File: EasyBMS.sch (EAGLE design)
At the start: 147 parts, among them Q1 BSS84LT1G, Q10 BSS84LT1G, Q11 BSS84LT1G, Q12 BSS84LT1G, Q14 BSS84LT1G, Q3 BSS84LT1G, Q4 BSS84LT1G, Q5 BSS84LT1G, Q6 BSS84LT1G, Q7 BSS84LT1G, Q8 BSS84LT1G, Q9 BSS84LT1G

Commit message: minimize board size to 100x32
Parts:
- removed JP10: (no value), pinhead:PINHD-1X10
- removed JP5, JP6: (no value), pinhead:PINHD-2X24
- removed JP7, JP8: (no value), pinhead:PINHD-1X24
- added JP11: (no value), pinhead_own:PINHD-2X24
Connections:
- removed net N$10: JP5.42, JP7.21
- removed net N$100: JP6.31, JP8.16
- removed net N$101: JP6.29, JP8.15
- removed net N$102: JP6.27, JP8.14
- removed net N$103: JP6.25, JP8.13
- removed net N$104: JP6.23, JP8.12
- removed net N$105: JP6.21, JP8.11
- removed net N$107: JP6.19, JP8.10
- removed net N$108: JP6.17, JP8.9
- removed net N$109: JP6.15, JP8.8
- removed net N$11: JP5.40, JP7.20
- removed net N$110: JP6.13, JP8.7
- removed net N$111: JP6.11, JP8.6
- removed net N$112: JP6.9, JP8.5
- removed net N$113: JP6.7, JP8.4
- removed net N$114: JP6.5, JP8.3
- removed net N$115: JP6.3, JP8.2
- removed net N$116: JP6.1, JP8.1
- removed net N$118: JP5.2, JP7.1
- removed net N$12: JP5.38, JP7.19
- removed net N$13: JP5.36, JP7.18
- removed net N$21: JP5.34, JP7.17
- removed net N$24: JP5.32, JP7.16
- removed net N$61: JP5.30, JP7.15
- removed net N$74: JP5.28, JP7.14
- removed net N$75: JP5.26, JP7.13
- removed net N$76: JP5.24, JP7.12
- removed net N$77: JP5.22, JP7.11
- removed net N$78: JP5.20, JP7.10
- removed net N$8: JP5.46, JP7.23
- removed net N$84: JP5.18, JP7.9
- removed net N$85: JP5.16, JP7.8
- removed net N$86: JP5.14, JP7.7
- removed net N$87: JP5.12, JP7.6
- removed net N$88: JP5.10, JP7.5
- removed net N$89: JP5.8, JP7.4
- removed net N$9: JP5.44, JP7.22
- removed net N$90: JP5.6, JP7.3
- removed net N$91: JP5.4, JP7.2
- removed net N$92: JP6.47, JP8.24
- removed net N$93: JP6.45, JP8.23
- removed net N$94: JP6.43, JP8.22
- removed net N$95: JP6.41, JP8.21
- removed net N$96: JP6.39, JP8.20
- removed net N$97: JP6.37, JP8.19
- removed net N$98: JP6.35, JP8.18
- removed net N$99: JP6.33, JP8.17
- new net C: C4.1, R19.1
- new net LOWER: C4.2, R17.1, R82.2
- new net S: R13.1
- new net UPPERCELL: Q1.S, R19.2
- net C0: now also JP11.46; no longer JP6.46
- net C1: now also JP11.47; no longer C4.1, JP5.47, R19.1
- net C10: now also JP11.11; no longer JP5.11
- net C11: now also JP11.7; no longer JP5.7
- net C12: now also JP11.3; no longer JP5.3
- net C2: now also JP11.43; no longer JP5.43
- net C3: now also JP11.39; no longer JP5.39
- net C4: now also JP11.35; no longer JP5.35
- net C5: now also JP11.31; no longer JP5.31
- net C6: now also JP11.27; no longer JP5.27
- net C7: now also JP11.23; no longer JP5.23
- net C8: now also JP11.19; no longer JP5.19
- net C9: now also JP11.15; no longer JP5.15
- net CSB: now also JP11.16; no longer JP6.16
- net DRIVE: now also JP11.22; no longer JP6.22
- net GND: now also JP11.18, JP11.36, JP11.38; no longer C4.2, C5.2, D3.A, JP10.1, JP10.10, JP10.2, JP10.3, JP10.4, JP10.5, JP10.6, JP10.7, JP10.8, JP10.9, JP6.18, JP6.36, JP6.38, R17.1, R3.2, R82.2
- net GPIO1: now also JP11.44; no longer JP6.44
- net GPIO2: now also JP11.42; no longer JP6.42
- net GPIO3: now also JP11.40; no longer JP6.40
- net GPIO4: now also JP11.34; no longer JP6.34
- net GPIO5: now also JP11.32; no longer JP6.32
- net ICMP: now also JP11.6, JP11.8; no longer JP6.6, JP6.8
- net IMB: now also JP11.4; no longer JP6.4
- net IPB: now also JP11.2; no longer JP6.2
- net MISO: now also JP11.10; no longer JP6.10
- net MOSI: now also JP11.12; no longer JP6.12
- net N$7: now also R3.2; no longer JP5.48, JP7.24
- net P13: now also JP11.1; no longer JP5.1
- net P2: no longer D3.K, Q1.S, R19.2
- net S1: now also JP11.48; no longer JP6.48, R13.1
- net S10: now also JP11.13; no longer JP5.13
- net S11: now also JP11.9; no longer JP5.9
- net S12: now also JP11.5; no longer JP5.5
- net S2: now also JP11.45; no longer JP5.45
- net S3: now also JP11.41; no longer JP5.41
- net S4: now also JP11.37; no longer JP5.37
- net S5: now also JP11.33; no longer JP5.33
- net S6: now also JP11.29; no longer JP5.29
- net S7: now also JP11.25; no longer JP5.25
- net S8: now also JP11.21; no longer JP5.21
- net S9: now also JP11.17; no longer JP5.17
- net SCK: now also JP11.14; no longer JP6.14
- net SWTEN: now also JP11.26; no longer JP6.26
- net VREF1: now also JP11.28; no longer JP6.28
- net VREF2: now also JP11.30; no longer JP6.30
- net VREG: now also JP11.24; no longer JP6.24
- net WDT: now also JP11.20; no longer JP6.20
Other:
- moved on the sheet: C5, R3

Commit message: size changed to 100x49
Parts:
- removed C4: (no value), rcl:C-EUC0402
- removed LED10, LED18: KT-0603R, led:LEDCHIPLED_0603
- removed Q1, Q14: BSS84LT1G, SamacSys_Parts:BSS84LT1G
- removed R100, R19: 100R, rcl:R-EU_R0402
- removed R13, R98: 3.3k, rcl:R-EU_R0402
- removed R17, R18, R9, R96, R97: 10R0, rcl:R-EU_R1206
- removed R82, R99: 470R, rcl:R-EU_R0402
- added C16: (no value), rcl:C-EUC0402
- added LED17, LED5: KT-0603R, led:LEDCHIPLED_0603
- added Q13, Q2: BSS84LT1G, SamacSys_Parts:BSS84LT1G
- added R10, R93: 3.3k, rcl:R-EU_R0402
- added R11, R94: 470R, rcl:R-EU_R0402
- added R4, R7, R8, R90, R91, R92: 10R0, rcl:R-EU_R1206
- added R89: 100R, rcl:R-EU_R0402
- R12, R24, R30, R36, R42, R48, R64, R70, R76, R83, R95: value 10R0 -> 100R; device rcl:R-EU_R1206 -> rcl:R-EU_R0402
- R21, R27, R33, R39, R45, R51, R67, R73, R79, R86: value 3.3k -> 10R0; device rcl:R-EU_R0402 -> rcl:R-EU_R1206
- R22, R28, R34, R40, R46, R52, R68, R74, R80, R87: value 470R -> 3.3k
- R23, R29, R35, R41, R47, R63, R69, R75, R81, R88: value 100R -> 470R
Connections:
- removed net C: C4.1, R19.1
- removed net LOWER: C4.2, R17.1, R82.2
- removed net N$15: R18.2, R9.1
- removed net N$157: LED10.C, R82.1
- removed net N$17: R17.2, R18.1
- removed net N$18: LED10.A, Q1.D, R9.2
- removed net N$25: Q1.G, R13.2
- removed net N$27 (its old number): LED7.A, Q4.D, R26.2
- removed net N$33 (its old number): LED8.A, Q5.D, R32.2
- removed net N$38 (its old number): LED9.A, Q6.D, R38.2
- removed net N$43 (its old number): LED11.A, Q7.D, R44.2
- removed net N$48 (its old number): LED12.A, Q8.D, R50.2
- removed net N$53 (its old number): LED13.A, Q9.D, R66.2
- removed net N$58 (its old number): LED14.A, Q10.D, R72.2
- removed net N$7: R3.2
- removed net N$79: R95.2, R96.1
- removed net N$80: R96.2, R97.1
- removed net N$81: LED18.A, Q14.D, R97.2
- removed net N$82: Q14.G, R98.2
- removed net N$83: LED18.C, R99.1
- removed net S: R13.1
- removed net UPPERCELL: Q1.S, R19.2
- new net N$10: LED5.A, Q2.D, R8.2
- new net N$11: Q2.G, R10.2
- new net N$12: LED5.C, R11.1
- new net N$16: LED6.A, Q3.D, R21.2
- new net N$24: Q4.G, R28.2
- new net N$26: LED7.C, R29.1
- new net N$32: LED8.C, R35.1
- new net N$37: LED9.C, R41.1
- new net N$42: LED11.C, R47.1
- new net N$47: LED12.C, R63.1
- new net N$52: LED13.C, R69.1
- new net N$57: LED14.C, R75.1
- new net N$61: Q11.G, R80.2
- new net N$68: R90.2, R91.1
- new net N$74: LED17.C, R94.1
- new net N$8: R4.2, R7.1
- new net N$9: R7.2, R8.1
- net C1: now also C6.1, R12.1
- net C10: now also C15.1, R83.1; no longer C17.1, R100.1
- net C11: now also C16.1, R89.1; no longer C12.1, R69.1
- net C12: now also C17.1, R95.1; no longer C14.1, R81.1
- net C2: now also C7.1, R24.1; no longer C6.1, R23.1
- net C3: now also C9.1, R36.1; no longer C7.1, R29.1
- net C4: now also R30.1; no longer R35.1
- net C5: now also C10.1, R42.1; no longer C9.1, R41.1
- net C6: now also C11.1, R48.1; no longer C10.1, R47.1
- net C7: now also C12.1, R64.1; no longer C11.1, R63.1
- net C8: now also R70.1; no longer R75.1
- net C9: now also C14.1, R76.1; no longer C15.1, R88.1
- net GND: now also C5.2, C6.2, D3.A, R11.2, R3.2, R4.1
- net N$14: now also R20.2, R21.1; no longer R12.2, R14.1
- net N$19: now also Q3.G, R22.2; no longer LED6.A, Q3.D, R20.2
- net N$20: now also LED6.C, R23.1; no longer Q3.G, R21.2
- net N$22: now also R26.2, R27.1; no longer LED6.C, R22.1
- net N$23: now also LED7.A, Q4.D, R27.2; no longer R24.2, R25.1
- net N$28: now also R32.2, R33.1; no longer Q4.G, R27.2
- net N$29: now also LED8.A, Q5.D, R33.2; no longer LED7.C, R28.1
- net N$31: now also Q5.G, R34.2; no longer R30.2, R31.1
- net N$34: now also R38.2, R39.1; no longer Q5.G, R33.2
- net N$35: now also LED9.A, Q6.D, R39.2; no longer LED8.C, R34.1
- net N$36: now also Q6.G, R40.2; no longer R36.2, R37.1
- net N$39: now also R44.2, R45.1; no longer Q6.G, R39.2
- net N$40: now also LED11.A, Q7.D, R45.2; no longer LED9.C, R40.1
- net N$41: now also Q7.G, R46.2; no longer R42.2, R43.1
- net N$44: now also R50.2, R51.1; no longer Q7.G, R45.2
- net N$45: now also LED12.A, Q8.D, R51.2; no longer LED11.C, R46.1
- net N$46: now also Q8.G, R52.2; no longer R48.2, R49.1
- net N$49: now also R66.2, R67.1; no longer Q8.G, R51.2
- net N$50: now also LED13.A, Q9.D, R67.2; no longer LED12.C, R52.1
- net N$51: now also Q9.G, R68.2; no longer R64.2, R65.1
- net N$54: now also R72.2, R73.1; no longer Q9.G, R67.2
- net N$55: now also LED14.A, Q10.D, R73.2; no longer LED13.C, R68.1
- net N$56: now also Q10.G, R74.2; no longer R70.2, R71.1
- net N$59: now also R78.2, R79.1; no longer Q10.G, R73.2
- net N$60: now also LED15.A, Q11.D, R79.2; no longer LED14.C, R74.1
- net N$62: now also LED15.C, R81.1; no longer R76.2, R77.1
- net N$64: now also R85.2, R86.1; no longer LED15.A, Q11.D, R78.2
- net N$65: now also LED16.A, Q12.D, R86.2; no longer Q11.G, R79.2
- net N$66: now also Q12.G, R87.2; no longer LED15.C, R80.1
- net N$67: now also LED16.C, R88.1; no longer R83.2, R84.1
- net N$69: now also R91.2, R92.1; no longer LED16.A, Q12.D, R85.2
- net N$71: now also LED17.A, Q13.D, R92.2; no longer Q12.G, R86.2
- net N$72: now also Q13.G, R93.2; no longer LED16.C, R87.1
- net P10: now also C15.2, Q10.S, R76.2, R77.1, R81.2; no longer C17.2, Q12.S, R88.2, R95.1, R99.2
- net P11: now also C16.2, Q11.S, R83.2, R84.1, R88.2; no longer C12.2, Q14.S, R100.2, R64.1, R68.2
- net P12: now also C17.2, Q12.S, R89.2, R90.1, R94.2; no longer C14.2, Q9.S, R69.2, R76.1, R80.2
- net P13: now also Q13.S, R95.2; no longer Q11.S, R81.2
- net P2: now also C7.2, D3.K, Q2.S, R12.2, R14.1, R23.2; no longer C6.2, R12.1, R22.2
- net P3: now also C9.2, R24.2, R31.1, R35.2; no longer C7.2, R23.2, R24.1, R28.2
- net P4: now also Q5.S, R25.1, R36.2; no longer Q4.S, R30.1, R34.2
- net P5: now also C10.2, Q4.S, R30.2, R37.1, R41.2; no longer C9.2, Q5.S, R35.2, R36.1, R40.2
- net P6: now also C11.2, R42.2, R43.1, R47.2; no longer C10.2, R41.2, R42.1, R46.2
- net P7: now also C12.2, R48.2, R49.1, R63.2; no longer C11.2, R47.2, R48.1, R52.2
- net P8: now also R64.2, R65.1, R69.2; no longer R63.2, R70.1, R74.2
- net P9: now also C14.2, Q9.S, R70.2, R71.1; no longer C15.2, Q10.S, R83.1, R87.2
- net S1: now also R10.1
- net S10: now also R80.1; no longer R98.1
- net S11: now also R87.1; no longer R67.1
- net S12: now also R93.1; no longer R79.1
- net S2: now also R22.1; no longer R21.1
- net S3: now also R34.1; no longer R27.1
- net S4: now also R28.1; no longer R33.1
- net S5: now also R40.1; no longer R39.1
- net S6: now also R46.1; no longer R45.1
- net S7: now also R52.1; no longer R51.1
- net S8: now also R68.1; no longer R73.1
- net S9: now also R74.1; no longer R86.1
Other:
- moved on the sheet: C10, C11, C12, C13, C14, C15, C17, C5, C6, C7, C8, C9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

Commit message: new 2x20 header used
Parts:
- removed JP11: (no value), pinhead_own:PINHD-2X24
- removed JP4, JP9: (no value), pinhead_own:PINHD-1X2
- added JP5: (no value), pinhead:PINHD-2X20
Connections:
- removed net DRIVE: JP11.22
- removed net N$117: JP9.1, R1.2
- removed net SWTEN: JP11.26
- removed net VREG: JP11.24, JP4.2
- removed net WDT: JP11.20
- net 5VDC: now also JP5.10, R1.2; no longer JP4.1, JP9.2
- net C0: now also JP5.30; no longer JP11.46
- net C1: now also JP5.34; no longer JP11.47
- net C10: now also JP5.11; no longer JP11.11
- net C11: now also JP5.7; no longer JP11.7
- net C12: now also JP5.3; no longer JP11.3
- net C2: now also JP5.38; no longer JP11.43
- net C3: now also JP5.39; no longer JP11.39
- net C4: now also JP5.35; no longer JP11.35
- net C5: now also JP5.31; no longer JP11.31
- net C6: now also JP5.27; no longer JP11.27
- net C7: now also JP5.23; no longer JP11.23
- net C8: now also JP5.19; no longer JP11.19
- net C9: now also JP5.15; no longer JP11.15
- net CSB: now also JP5.8; no longer JP11.16
- net GND: now also JP5.16, JP5.18; no longer JP11.18, JP11.36, JP11.38
- net GPIO1: now also JP5.28; no longer JP11.44
- net GPIO2: now also JP5.26; no longer JP11.42
- net GPIO3: now also JP5.24; no longer JP11.40
- net GPIO4: now also JP5.22; no longer JP11.34
- net GPIO5: now also JP5.20; no longer JP11.32
- net ICMP: no longer JP11.6, JP11.8
- net IMB: no longer JP11.4
- net IPB: no longer JP11.2
- net MISO: now also JP5.2; no longer JP11.10
- net MOSI: now also JP5.4; no longer JP11.12
- net P13: now also JP5.1; no longer JP11.1
- net S1: now also JP5.32; no longer JP11.48
- net S10: now also JP5.13; no longer JP11.13
- net S11: now also JP5.9; no longer JP11.9
- net S12: now also JP5.5; no longer JP11.5
- net S2: now also JP5.36; no longer JP11.45
- net S3: now also JP5.40; no longer JP11.41
- net S4: now also JP5.37; no longer JP11.37
- net S5: now also JP5.33; no longer JP11.33
- net S6: now also JP5.29; no longer JP11.29
- net S7: now also JP5.25; no longer JP11.25
- net S8: now also JP5.21; no longer JP11.21
- net S9: now also JP5.17; no longer JP11.17
- net SCK: now also JP5.6; no longer JP11.14
- net VREF1: now also JP5.12; no longer JP11.28
- net VREF2: now also JP5.14; no longer JP11.30

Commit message: positioning
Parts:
- added C18, C19, C4: (no value), rcl:C-EUC1206
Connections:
- net 5VDC: now also C19.1
- net GND: now also C18.2, C19.2, C4.2
- net VREF1: now also C18.1
- net VREF2: now also C4.1
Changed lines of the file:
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@@
 <part name="R95" library="rcl" library_urn="urn:adsk.eagle:library:334" deviceset="R-EU_" device="R0402" package3d_urn="urn:adsk.eagle:package:23547/1" value="100R"/>
 <part name="JP5" library="pinhead" library_urn="urn:adsk.eagle:library:325" deviceset="PINHD-2X20" device="" package3d_urn="urn:adsk.eagle:package:22443/2"/>
+<part name="C4" library="rcl" library_urn="urn:adsk.eagle:library:334" deviceset="C-EU" device="C1206" package3d_urn="urn:adsk.eagle:package:23618/2"/>
+<part name="C18" library="rcl" library_urn="urn:adsk.eagle:library:334" deviceset="C-EU" device="C1206" package3d_urn="urn:adsk.eagle:package:23618/2"/>
+<part name="C19" library="rcl" library_urn="urn:adsk.eagle:library:334" deviceset="C-EU" device="C1206" package3d_urn="urn:adsk.eagle:package:23618/2"/>
 </parts>
 <sheets>
@@
 <attribute name="NAME" x="130.81" y="346.075" size="1.778" layer="95"/>
 <attribute name="VALUE" x="130.81" y="289.56" size="1.778" layer="96"/>
+</instance>
+<instance part="C4" gate="G$1" x="139.7" y="30.48" smashed="yes">
+<attribute name="NAME" x="141.224" y="30.861" size="1.778" layer="95"/>
+<attribute name="VALUE" x="141.224" y="25.781" size="1.778" layer="96"/>
+</instance>
+<instance part="C18" gate="G$1" x="172.72" y="30.48" smashed="yes">
+<attribute name="NAME" x="174.244" y="30.861" size="1.778" layer="95"/>
+<attribute name="VALUE" x="174.244" y="25.781" size="1.778" layer="96"/>
+</instance>
+<instance part="C19" gate="G$1" x="205.74" y="30.48" smashed="yes">
+<attribute name="NAME" x="207.264" y="30.861" size="1.778" layer="95"/>
+<attribute name="VALUE" x="207.264" y="25.781" size="1.778" layer="96"/>
 </instance>
 </instances>
@@
 <wire x1="187.96" y1="43.18" x2="177.8" y2="43.18" width="0.1524" layer="91"/>
 <pinref part="R1" gate="G$1" pin="2"/>
+<pinref part="C19" gate="G$1" pin="1"/>
+<wire x1="205.74" y1="33.02" x2="198.12" y2="33.02" width="0.1524" layer="91"/>
+<junction x="198.12" y="33.02"/>
 </segment>
 <segment>
@@
 <wire x1="91.44" y1="17.78" x2="91.44" y2="-22.86" width="0.1524" layer="91"/>
 <wire x1="91.44" y1="-22.86" x2="149.86" y2="-22.86" width="0.1524" layer="91"/>
+<pinref part="C4" gate="G$1" pin="2"/>
+<wire x1="139.7" y1="25.4" x2="149.86" y2="25.4" width="0.1524" layer="91"/>
+<junction x="149.86" y="25.4"/>
+<pinref part="C18" gate="G$1" pin="2"/>
+<wire x1="172.72" y1="25.4" x2="165.1" y2="25.4" width="0.1524" layer="91"/>
+<junction x="165.1" y="25.4"/>
+<pinref part="C19" gate="G$1" pin="2"/>
+<wire x1="205.74" y1="25.4" x2="198.12" y2="25.4" width="0.1524" layer="91"/>
+<junction x="198.12" y="25.4"/>
 </segment>
 <segment>
@@
 <wire x1="165.1" y1="50.8" x2="165.1" y2="33.02" width="0.1524" layer="91"/>
 <label x="165.1" y="45.72" size="1.778" layer="95"/>
+<pinref part="C18" gate="G$1" pin="1"/>
+<wire x1="165.1" y1="33.02" x2="172.72" y2="33.02" width="0.1524" layer="91"/>
+<junction x="165.1" y="33.02"/>
 </segment>
 <segment>
@@
 <wire x1="149.86" y1="48.26" x2="149.86" y2="33.02" width="0.1524" layer="91"/>
 <label x="149.86" y="45.72" size="1.778" layer="95"/>
-</segment>
-<segment>
+<pinref part="C4" gate="G$1" pin="1"/>
+<wire x1="149.86" y1="33.02" x2="139.7" y2="33.02" width="0.1524" layer="91"/>
+<junction x="149.86" y="33.02"/>
+</segment>
+<segment>

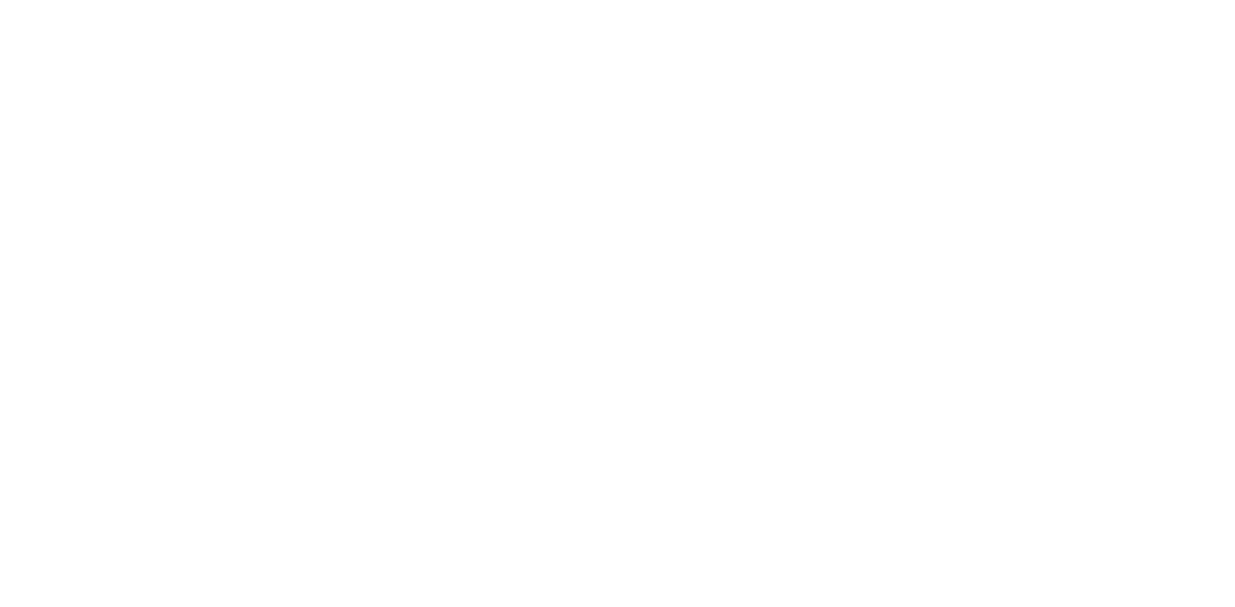
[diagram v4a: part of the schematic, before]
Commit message: extension ports added
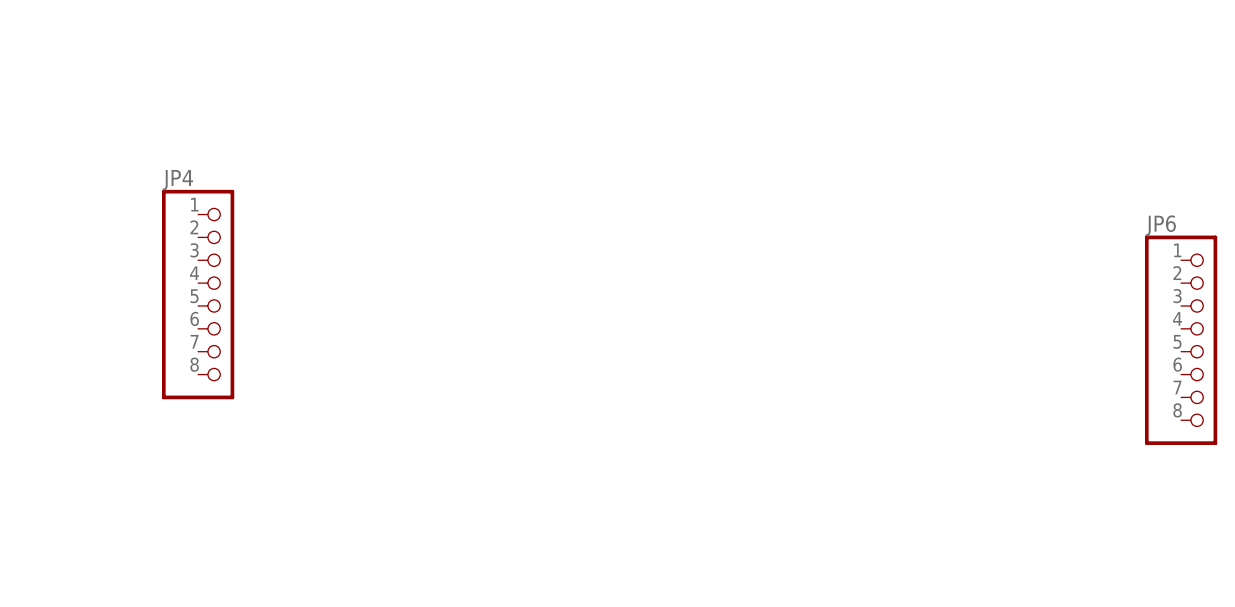
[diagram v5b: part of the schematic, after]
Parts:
- added JP4, JP6: (no value), pinhead:PINHD-1X8
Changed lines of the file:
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@@
 <part name="C18" library="rcl" library_urn="urn:adsk.eagle:library:334" deviceset="C-EU" device="C1206" package3d_urn="urn:adsk.eagle:package:23618/2"/>
 <part name="C19" library="rcl" library_urn="urn:adsk.eagle:library:334" deviceset="C-EU" device="C1206" package3d_urn="urn:adsk.eagle:package:23618/2"/>
+<part name="JP4" library="pinhead" library_urn="urn:adsk.eagle:library:325" deviceset="PINHD-1X8" device="" package3d_urn="urn:adsk.eagle:package:22409/2"/>
+<part name="JP6" library="pinhead" library_urn="urn:adsk.eagle:library:325" deviceset="PINHD-1X8" device="" package3d_urn="urn:adsk.eagle:package:22409/2"/>
 </parts>
 <sheets>
@@
 <attribute name="VALUE" x="207.264" y="25.781" size="1.778" layer="96"/>
 </instance>
+<instance part="JP4" gate="A" x="462.28" y="248.92" smashed="yes">
+<attribute name="NAME" x="455.93" y="262.255" size="1.778" layer="95"/>
+<attribute name="VALUE" x="455.93" y="236.22" size="1.778" layer="96"/>
+</instance>
+<instance part="JP6" gate="A" x="571.5" y="243.84" smashed="yes">
+<attribute name="NAME" x="565.15" y="257.175" size="1.778" layer="95"/>
+<attribute name="VALUE" x="565.15" y="231.14" size="1.778" layer="96"/>
+</instance>
 </instances>
